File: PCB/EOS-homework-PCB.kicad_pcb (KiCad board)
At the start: 4 copper layers, 100 x 100 mm, 72 parts, among them J1 STDC-14 Debug, J2 5V, J3 CAN, J4 USB-C MCU, J5 EdgeConn_FC, Q1 2N7002, SW1 Reset, U1 ADM1818, U2 W25N512GVEIG, U3 STM32G473RCTx, U4 AP2112K-3.3, U5 MAX40200AUK, U6 MCP2562-E-SN, U7 USBLC6-2SC6, Y1 16MHz/8pF

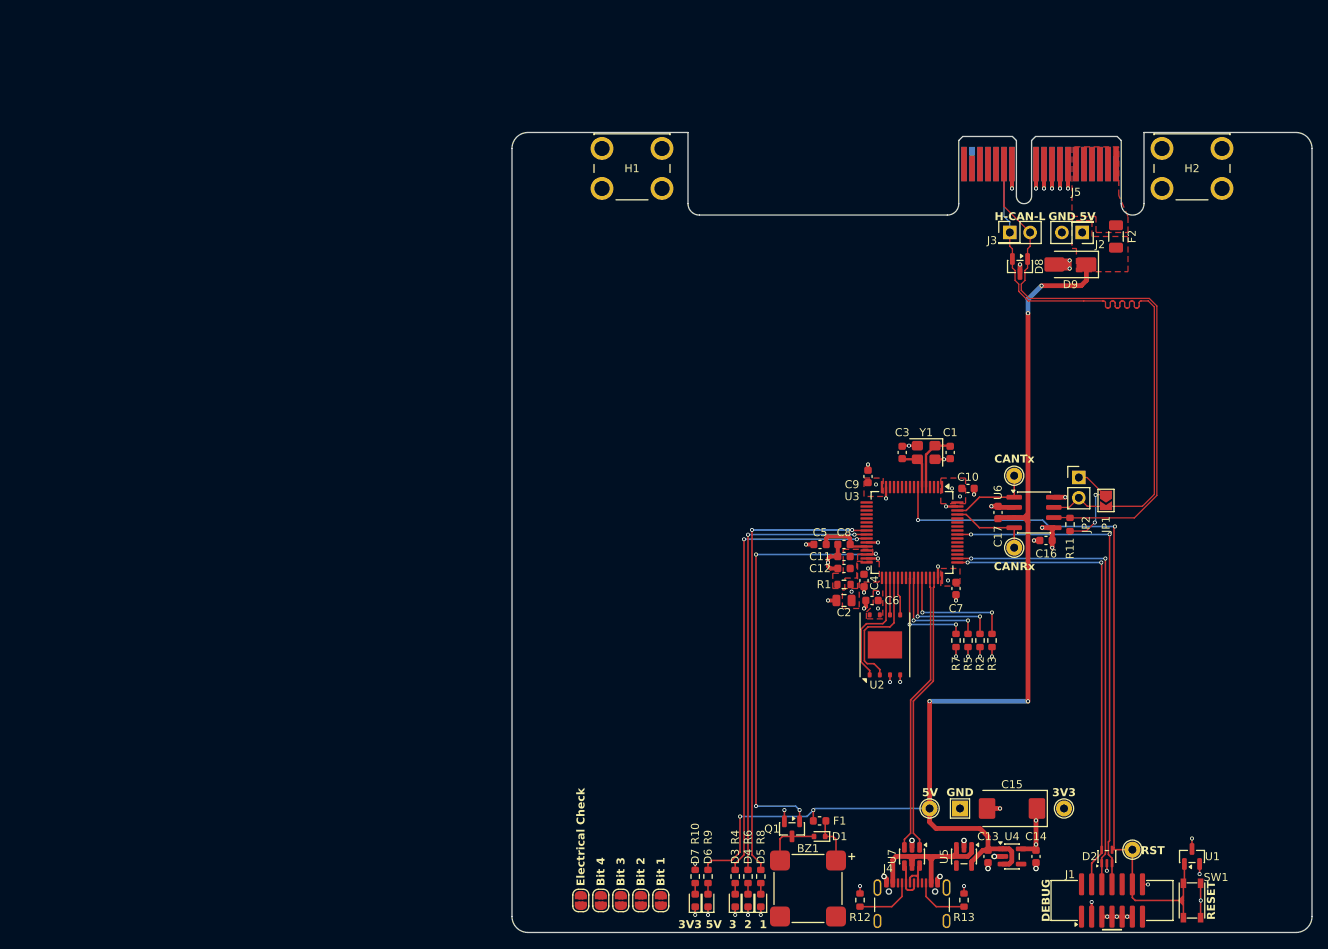
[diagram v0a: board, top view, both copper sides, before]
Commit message: Schematic done
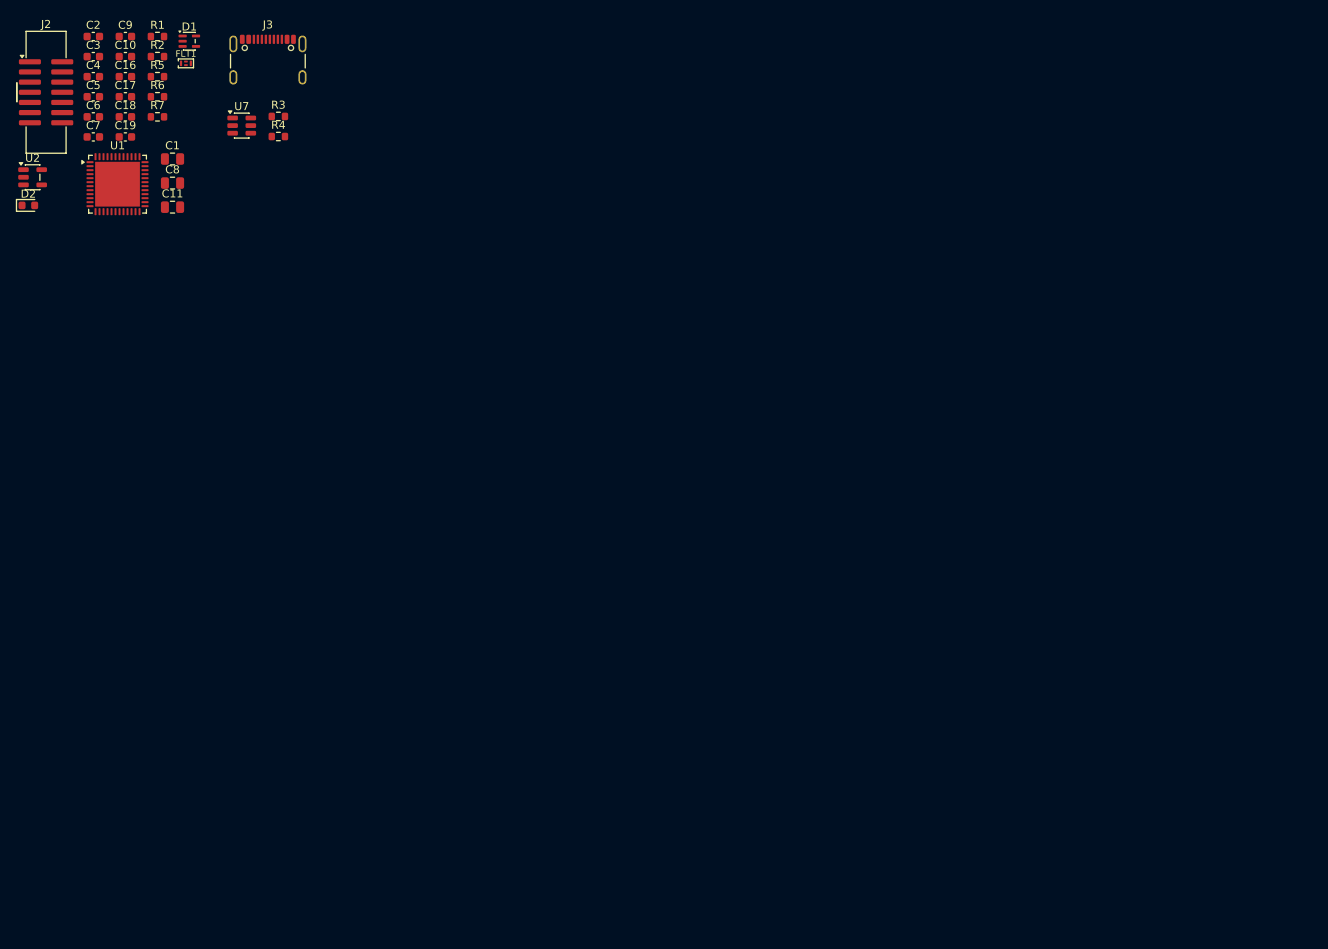
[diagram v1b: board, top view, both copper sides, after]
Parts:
- removed BZ1: Buzzer, kicad-standard-lib:Buzzer_CUI_CMT-8504-100-SMT-TR
- removed C12, C13, C14: 1u/16V, Capacitor_SMD:C_0603_1608Metric
- removed C15: 100u/6.3V, Capacitor_Tantalum_SMD:CP_EIA-7343-20_Kemet-V
- removed D3, D6, D7: Red, LED_SMD:LED_0603_1608Metric
- removed D4: Yellow, LED_SMD:LED_0603_1608Metric
- removed D5: Green, LED_SMD:LED_0603_1608Metric
- removed D8: CAN TVS, Package_TO_SOT_SMD:SOT-23
- removed D9: 5.0V, Diode_SMD:D_SMA
- removed F1: 250mA/9V, Fuse:Fuse_0603_1608Metric
- removed F2: 1A/6V, Fuse:Fuse_1206_3216Metric
- removed H1, H2: 7790_NC, kicad-standard-lib:Mounting_Keystone_7790_NC
- removed J1: STDC-14 Debug, kicad-standard-lib:IDC-Header_2x07_P1.27mm_Vertical_SMD
- removed J4: USB-C MCU, Connector_USB:USB_C_Receptacle_GCT_USB4105-xx-A_16P_TopMnt_Horizontal
- removed J5: EdgeConn_FC, Connector_PCBEdge:BUS_PCIexpress_x1
- removed JP1: Termination, Jumper:SolderJumper-2_P1.3mm_Open_TrianglePad1.0x1.5mm
- removed JP2: DebugTermination, Connector_PinHeader_2.54mm:PinHeader_1x02_P2.54mm_Vertical
- removed JP3: Assembly Done, Jumper:SolderJumper-2_P1.3mm_Open_RoundedPad1.0x1.5mm
- removed JP4: Numbering 1, Jumper:SolderJumper-2_P1.3mm_Open_RoundedPad1.0x1.5mm
- removed JP5: Numbering 2, Jumper:SolderJumper-2_P1.3mm_Open_RoundedPad1.0x1.5mm
- removed JP6: Numbering 3, Jumper:SolderJumper-2_P1.3mm_Open_RoundedPad1.0x1.5mm
- removed JP7: Numbering 4, Jumper:SolderJumper-2_P1.3mm_Open_RoundedPad1.0x1.5mm
- removed Q1: 2N7002, Package_TO_SOT_SMD:SOT-23
- removed R10, R8, R9: 1k, Resistor_SMD:R_0603_1608Metric
- removed R11: 120R, Resistor_SMD:R_0603_1608Metric
- removed R12, R13: 5k1, Resistor_SMD:R_0603_1608Metric
- removed SW1: Reset, kicad-standard-lib:SW_Push_Wuerth_434123025826
- removed TP1, TP2, TP3, TP4, TP5: TestPoint, TestPoint:TestPoint_THTPad_D2.0mm_Drill1.0mm
- removed TP6: TestPoint, TestPoint:TestPoint_THTPad_2.0x2.0mm_Drill1.0mm
- removed U3: STM32G473RCTx, Package_QFP:LQFP-64_10x10mm_P0.5mm
- removed U4: AP2112K-3.3, Package_TO_SOT_SMD:SOT-23-5
- removed U5: MAX40200AUK, Package_TO_SOT_SMD:SOT-23-5
- removed U6: MCP2562-E-SN, Package_SO:SOIC-8_3.9x4.9mm_P1.27mm
- removed Y1: 16MHz/8pF, Crystal:Crystal_SMD_3225-4Pin_3.2x2.5mm
- added C18: 1u/50V, Capacitor_SMD:C_0603_1608Metric, F.Cu at (51.7, 48.0)
- added C19: 1u/50V, Capacitor_SMD:C_0603_1608Metric, F.Cu at (51.7, 50.6)
- added FLT1: DLF162500LT-5028A1, OzelHD-addition-repo_FP:DLF162500LT-5028A1, F.Cu at (59.2, 41.4)
- C1: value 10p/50V -> 4u7/16V; footprint Capacitor_SMD:C_0603_1608Metric -> Capacitor_SMD:C_0805_2012Metric
- C11: value 10n/50V -> 4u7/16V; footprint Capacitor_SMD:C_0603_1608Metric -> Capacitor_SMD:C_0805_2012Metric
- C2: value 10u/10V -> 100n/50V; footprint Capacitor_SMD:C_0805_2012Metric -> Capacitor_SMD:C_0603_1608Metric
- C3: value 10p/50V -> 100n/50V
- C5: value 1u/16V -> 100n/50V
- C8: value 100n/50V -> 4u7/16V; footprint Capacitor_SMD:C_0603_1608Metric -> Capacitor_SMD:C_0805_2012Metric
- D1: value 10V -> 82402374; footprint Diode_SMD:D_SOD-523 -> Package_TO_SOT_SMD:SOT-353_SC-70-5
- D2: value 82402374 -> Green; footprint Package_TO_SOT_SMD:SOT-353_SC-70-5 -> LED_SMD:LED_0603_1608Metric
- J2: value 5V -> Conn_ST_STDC14; footprint Connector_PinHeader_2.54mm:PinHeader_2x01_P2.54mm_Vertical -> kicad-standard-lib:IDC-Header_2x07_P1.27mm_Vertical_SMD
- J3: value CAN -> USB-C MCU; footprint Connector_PinHeader_2.54mm:PinHeader_2x01_P2.54mm_Vertical -> Connector_USB:USB_C_Receptacle_GCT_USB4105-xx-A_16P_TopMnt_Horizontal
- R1: value 0R -> 10k
- R2, R5: value 2k2 -> 100R
- R3: value 2k2 -> 5k1
- R4: value 1k -> 5k1
- R6: value 1k -> 100R
- R7: value 2k2 -> 1k
- U1: value ADM1818 -> STM32WB55CEU6; footprint Package_TO_SOT_SMD:SOT-23 -> Package_DFN_QFN:QFN-48-1EP_7x7mm_P0.5mm_EP5.6x5.6mm
- U2: value W25N512GVEIG -> MIC5365-3.3YD5; footprint kicad-standard-lib:WSON-8-1EP_8x6mm_P1.27mm_EP3.4x4.3mm -> Package_TO_SOT_SMD:TSOT-23-5
- moved U1 158.4 mm to (50.7, 56.5), turned to 0 degrees
- moved D2 157.5 mm to (39.5, 59.1), turned to 0 degrees
- moved J2 130.7 mm to (41.8, 45.0), turned to 0 degrees
- moved C16 128.9 mm to (51.7, 43.0), turned to 0 degrees
- moved D1 126.8 mm to (59.7, 38.6), turned to 0 degrees
- moved R2 126.1 mm to (55.7, 40.5), turned to 0 degrees
- moved U7 124.0 mm to (66.2, 49.1), turned to 0 degrees
- moved R5 123.4 mm to (55.7, 43.0), turned to 0 degrees
- moved R6 122.3 mm to (55.7, 45.5), turned to 0 degrees
- moved C7 121.7 mm to (47.7, 50.6), turned to 0 degrees
- moved U2 121.5 mm to (40.1, 55.6), turned to 0 degrees
- moved C17 120.8 mm to (51.7, 45.5), turned to 0 degrees
- moved R7 119.4 mm to (55.7, 48.0), turned to 0 degrees
- moved C10 118.4 mm to (51.7, 40.5)
- moved C2 117.4 mm to (47.7, 38.0), turned to 0 degrees
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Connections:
- C1 pad 1: /Microcontroller/OSC_IN -> +3.3V
- C11 pad 1: +3.3VA -> /Microcontroller/SMPSFB
- C16 pad 1: +3.3V -> /Microcontroller/~{Reset}
- C17 pad 1: +5V -> /Microcontroller/BOOT0
- C3 pad 1: /Microcontroller/OSC_OUT -> +3.3V
- C5 pad 1: /Microcontroller/VREF -> +3.3V
- C8 pad 1: /Microcontroller/VREF -> +3.3V
- D1 pad 1: Net-(BZ1-+) -> /Microcontroller/SWO
- D1 pad 2: Net-(BZ1--) -> GND
- D2 pad 1: /Microcontroller/SWCLK -> Net-(D2-K)
- D2 pad 2: GND -> /Microcontroller/LED
- J2 pad 1: +5V -> unconnected-(J2-NC-Pad1)
- J2 pad 2: GND -> unconnected-(J2-NC-Pad2)
- R1 pad 1: +3.3VA -> /Microcontroller/BOOT0
- R1 pad 2: +3.3V -> GND
- R2 pad 1: +3.3V -> /Microcontroller/BOOT0
- R2 pad 2: /Microcontroller/I2C2.SDA -> Net-(R2-Pad2)
- R3 pad 1: +3.3V -> GND
- R3 pad 2: /Microcontroller/I2C2.SCL -> Net-(J3-CC1)
- R4 pad 1: /Microcontroller/LED3 -> GND
- R4 pad 2: Net-(D3-A) -> Net-(J3-CC2)
- R5 pad 1: +3.3V -> /Microcontroller/UART_TXC
- R5 pad 2: /Microcontroller/I2C3.SDA -> /Microcontroller/UART_TX
- R6 pad 1: /Microcontroller/LED2 -> /Microcontroller/UART_RX
- R6 pad 2: Net-(D4-A) -> /Microcontroller/UART_RXC
- R7 pad 1: +3.3V -> GND
- R7 pad 2: /Microcontroller/I2C3.SCL -> Net-(D2-K)
- U1 pad 1: /Microcontroller/~{Reset} -> +3.3V
- U1 pad 2: +3.3V -> /Microcontroller/LSE_IN
- U1 pad 3: GND -> /Microcontroller/LSE_OUT
- U2 pad 1: /Microcontroller/SPI2.CS -> +5V
- U2 pad 2: /Microcontroller/SPI2.MISO -> GND
- U2 pad 3: +3.3V -> +5V
- U2 pad 4: GND -> unconnected-(U2-NC-Pad4)
- U2 pad 5: /Microcontroller/SPI2.MOSI -> +3.3V
- U7 pad 1: /Microcontroller/USB+ -> /USB Connector/USB_D+
- U7 pad 3: /Microcontroller/USB- -> /USB Connector/USB_D-
- U7 pad 5: VBUS -> +5V
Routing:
- net +5V: track 145.0 -> 0.00 mm, vias 6 -> 0
- net GND: track 100.9 -> 0.00 mm, vias 51 -> 0
- net /Microcontroller/~{Reset}: track 91.5 -> 0.00 mm, vias 2 -> 0
- net /Backplane connector, mounting/CANH: track 77.1 -> 0.00 mm
- net /Backplane connector, mounting/CANL: track 72.8 -> 0.00 mm
- net /Microcontroller/SWO: track 63.0 -> 0.00 mm, vias 2 -> 0
- net /Microcontroller/SWCLK: track 59.4 -> 0.00 mm, vias 2 -> 0
- net /Microcontroller/SWDIO: track 58.8 -> 0.00 mm, vias 2 -> 0
- net /Microcontroller/LED1: track 57.3 -> 0.00 mm, vias 2 -> 0
- net /Microcontroller/LED3: track 57.1 -> 0.00 mm, vias 2 -> 0
- net /Microcontroller/LED2: track 56.7 -> 0.00 mm, vias 2 -> 0
- net /Microcontroller/Buzzer_PWM: track 54.7 -> 0.00 mm, vias 4 -> 0
- net /Microcontroller/USB-: track 35.1 -> 0.00 mm
- net /Microcontroller/USB+: track 35.1 -> 0.00 mm
- net VBUS: track 22.9 -> 0.00 mm
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- removed copper zone on F.Cu, net +3.3V
- removed copper zone on In2.Cu, net +3.3V
- removed copper zone on F.Cu, net +3.3VA
- removed copper zone on F.Cu, net +5V
- removed copper zone on F.Cu, net /Backplane connector, mounting/5V_prefuse
- removed copper zone on In1.Cu, net GND
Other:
- board outline removed
- board text removed: "3 2 1"
- board text removed: "3V3"
- board text removed: "3V3 5V"
- board text removed: "5V"
- board text removed: "Backplane PCB surface"
- board text removed: "Bit 1"
- board text removed: "Bit 2"
- board text removed: "Bit 3"
- board text removed: "Bit 4"
- board text removed: "CANRx"
- board text removed: "CANTx"
- board text removed: "Center: X=150 Y=100"
- board text removed: "DEBUG"
- board text removed: "Electrical Check"
- board text removed: "GND"
- board text removed: "GND 5V"
- board text removed: "H-CAN-L"
- board text removed: "RESET"
- board text removed: "RST"

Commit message: PCB done.
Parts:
- removed U7: USBLC6-2SC6, Package_TO_SOT_SMD:SOT-23-6
- added C12: 100n/50V, Capacitor_SMD:C_0603_1608Metric, F.Cu at (143.2, 103.5)
- added C13: 10p, Capacitor_SMD:C_0603_1608Metric, F.Cu at (143.2, 97.5)
- added C14: 4u7/16V, Capacitor_SMD:C_0805_2012Metric, F.Cu at (155.8, 103.3)
- added C15: 1u/50V, Capacitor_SMD:C_0603_1608Metric, F.Cu at (147.0, 89.0)
- added D3: Red, LED_SMD:LED_0603_1608Metric, F.Cu at (141.2, 80.2)
- added D4: Red, LED_SMD:LED_0603_1608Metric, F.Cu at (139.5, 80.2)
- added FID1: Fiducial, Fiducial:Fiducial_1mm_Mask2mm, F.Cu at (134.5, 85.0)
- added FID2: Fiducial, Fiducial:Fiducial_1mm_Mask2mm, F.Cu at (134.5, 109.0)
- added FID3: Fiducial, Fiducial:Fiducial_1mm_Mask2mm, F.Cu at (159.0, 109.0)
- added H1: MountingHole_Pad, MountingHole:MountingHole_2.2mm_M2_Pad_Via, F.Cu at (134.5, 81.2)
- added H2: MountingHole_Pad, MountingHole:MountingHole_2.2mm_M2_Pad_Via, F.Cu at (159.0, 81.2)
- added H3: MountingHole_Pad, MountingHole:MountingHole_2.2mm_M2_Pad_Via, F.Cu at (159.0, 113.8)
- added H4: MountingHole_Pad, MountingHole:MountingHole_2.2mm_M2_Pad_Via, F.Cu at (134.5, 113.8)
- added J1: Conn_ST_STDC14, kicad-standard-lib:IDC-Header_2x07_P1.27mm_Vertical_SMD, F.Cu at (135.2, 99.2)
- added J4: USB-C MCU, Connector_USB:USB_C_Receptacle_GCT_USB4105-xx-A_16P_TopMnt_Horizontal, F.Cu at (149.5, 81.5)
- added L1: 10n, Inductor_SMD:L_0402_1005Metric, F.Cu at (155.8, 101.0)
- added L2: 10u, Inductor_SMD:L_0805_2012Metric, F.Cu at (157.8, 102.0)
- added L3: 2n7, Inductor_SMD:L_0402_1005Metric, F.Cu at (151.2, 108.8)
- added R8: 1k, Resistor_SMD:R_0603_1608Metric, F.Cu at (141.2, 83.2)
- added R9: 1k, Resistor_SMD:R_0603_1608Metric, F.Cu at (139.5, 83.2)
- added SW1: Reset, kicad-standard-lib:SW_Push_Wuerth_434123025826, F.Cu at (159.0, 89.0)
- added TP1: TestPoint, TestPoint:TestPoint_Pad_D1.0mm, F.Cu at (159.1, 85.4)
- added TP2: TestPoint, TestPoint:TestPoint_Pad_D1.0mm, F.Cu at (140.0, 88.5)
- added TP3: TestPoint_Square, TestPoint:TestPoint_THTPad_1.5x1.5mm_Drill0.7mm, F.Cu at (160.5, 105.5)
- added U3: USBLC6-2SC6, Package_TO_SOT_SMD:SOT-23-6, F.Cu at (149.5, 89.0)
- added X1: 32MHz, Crystal:Crystal_SMD_2016-4Pin_2.0x1.6mm, F.Cu at (156.0, 106.8)
- added X2: 32kHz768, Crystal:Crystal_SMD_2012-2Pin_2.0x1.2mm, F.Cu at (144.0, 99.8)
- C11: value 4u7/16V -> 10p; footprint Capacitor_SMD:C_0805_2012Metric -> Capacitor_SMD:C_0603_1608Metric
- C16: value 100n/50V -> 0p8
- C17: value 100n/50V -> 0p3
- C18: value 1u/50V -> 100n/50V
- C6: value 100n/50V -> 4u7/16V; footprint Capacitor_SMD:C_0603_1608Metric -> Capacitor_SMD:C_0805_2012Metric
- C8: value 4u7/16V -> 100n/50V; footprint Capacitor_SMD:C_0805_2012Metric -> Capacitor_SMD:C_0603_1608Metric
- J2: value Conn_ST_STDC14 -> Conn_01x04; footprint kicad-standard-lib:IDC-Header_2x07_P1.27mm_Vertical_SMD -> Connector_Molex:Molex_PicoBlade_53048-0410_1x04_P1.25mm_Horizontal
- J3: value USB-C MCU -> Conn_Coaxial; footprint Connector_USB:USB_C_Receptacle_GCT_USB4105-xx-A_16P_TopMnt_Horizontal -> Connector_Coaxial:U.FL_Hirose_U.FL-R-SMT-1_Vertical
- R1: value 10k -> 1k
- R3: value 5k1 -> 100R
- R4: value 5k1 -> 10k
- R6: value 100R -> 5k1
- R7: value 1k -> 5k1
- moved C2 122.4 mm to (155.8, 95.5), turned to 90 degrees
- moved C3 122.2 mm to (149.2, 108.5), turned to 180 degrees
- moved C10 121.4 mm to (152.8, 107.8), turned to -90 degrees
- moved C6 121.1 mm to (157.8, 98.5), turned to 90 degrees
- moved C17 119.5 mm to (152.0, 110.5)
- moved J2 118.4 mm to (139.4, 112.0)
- moved C16 117.7 mm to (150.5, 107.0), turned to 180 degrees
- moved FLT1 116.2 mm to (151.2, 112.2), turned to -90 degrees
- moved C9 114.8 mm to (151.2, 95.2), turned to 90 degrees
- moved C4 113.9 mm to (143.2, 105.0), turned to 180 degrees
- moved C18 112.3 mm to (155.5, 90.8)
- moved J3 110.2 mm to (151.2, 115.9), turned to -90 degrees
- moved R5 109.9 mm to (155.5, 89.0)
- moved R2 109.8 mm to (143.2, 106.8)
- moved U2 109.6 mm to (144.5, 89.0), turned to 90 degrees
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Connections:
- C11 pad 1: /Microcontroller/SMPSFB -> /Microcontroller/LSE_OUT
- C16 pad 1: /Microcontroller/~{Reset} -> /Microcontroller/RF
- C17 pad 1: /Microcontroller/BOOT0 -> /Microcontroller/RF_MATCH
- C18 pad 1: +5V -> /Microcontroller/BOOT0
- D1 pad 5: /Microcontroller/~{Reset} -> /Microcontroller/SW_~{Reset}
- D2 pad 1: Net-(D2-K) -> GND
- D2 pad 2: /Microcontroller/LED -> Net-(D2-A)
- J2 pad 1: unconnected-(J2-NC-Pad1) -> +3.3V
- J2 pad 2: unconnected-(J2-NC-Pad2) -> /Microcontroller/UART_TXC
- J2 pad 3: +5V -> /Microcontroller/UART_RXC
- J2 pad 4: /Microcontroller/SWDIO -> GND
- R1 pad 1: /Microcontroller/BOOT0 -> Net-(D2-A)
- R1 pad 2: GND -> /Microcontroller/LED
- R2 pad 1: /Microcontroller/BOOT0 -> /Microcontroller/UART_TXC
- R2 pad 2: Net-(R2-Pad2) -> /Microcontroller/UART_TX
- R3 pad 1: GND -> /Microcontroller/UART_RX
- R3 pad 2: Net-(J3-CC1) -> /Microcontroller/UART_RXC
- R4 pad 1: GND -> /Microcontroller/BOOT0
- R4 pad 2: Net-(J3-CC2) -> GND
- R5 pad 1: /Microcontroller/UART_TXC -> /Microcontroller/BOOT0
- R5 pad 2: /Microcontroller/UART_TX -> Net-(R5-Pad2)
- R6 pad 1: /Microcontroller/UART_RX -> GND
- R6 pad 2: /Microcontroller/UART_RXC -> Net-(J4-CC1)
- R7 pad 2: Net-(D2-K) -> Net-(J4-CC2)
- U1 pad 7: /Microcontroller/~{Reset} -> /Microcontroller/SW_~{Reset}
- U2 pad 1: +5V -> VBUS
- U2 pad 3: +5V -> VBUS
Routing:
- net GND: track 0.00 -> 50.9 mm, vias 0 -> 57
- net +3.3V: track 0.00 -> 44.9 mm, vias 0 -> 14
- net /Microcontroller/LED: track 0.00 -> 33.5 mm, vias 0 -> 2
- net VBUS: track 0.00 -> 28.6 mm, vias 0 -> 4
- net /Microcontroller/BOOT0: track 0.00 -> 21.4 mm, vias 0 -> 2
- net /Microcontroller/SW_~{Reset}: track 0.00 -> 20.4 mm, vias 0 -> 2
- net /Microcontroller/SWDIO: track 0.00 -> 19.1 mm, vias 0 -> 2
- net /Microcontroller/SWO: track 0.00 -> 17.9 mm, vias 0 -> 2
- net /Microcontroller/SWCLK: track 0.00 -> 16.8 mm, vias 0 -> 2
- net /Microcontroller/USB_D-: track 0.00 -> 10.4 mm
- net /Microcontroller/USB_D+: track 0.00 -> 10.4 mm
- net Net-(J4-CC1): track 0.00 -> 6.98 mm
- net /Microcontroller/UART_TXC: track 0.00 -> 6.88 mm
- net Net-(J4-CC2): track 0.00 -> 6.48 mm
- net /Microcontroller/UART_RX: track 0.00 -> 5.94 mm
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- added copper zone on In2.Cu, net +3.3V
- added copper zone on In1.Cu, net GND
- added copper zone on F.Cu, net VBUS
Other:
- board outline added: 31 x 39.5 mm
- board text added: "."
- board text added: ". VBUS .. +3V3 ... GPIO16"
- board text added: ".."
- board text added: "..."
- board text added: "3V3"
- board text added: "GND"
- board text added: "Homework PCB dcarocci 29.09.26"
- board text added: "RST"
- board text added: "VBUS"
